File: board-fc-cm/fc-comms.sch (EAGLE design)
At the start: 251 parts, among them IC1 TPS79930QDDCRQ1, IC10 LNA_COMMON, IC11 MPU-9250, IC12 TXB0108PW, IC13 TPS3813K33-EP_DBV_6, IC14 TMP100-EP_DBV_6, IC15 LHA1+, IC16 PCT2075TP, IC17 MMZ09332BT1, IC18 PCT2075TP, IC2 TPS79930QDDCRQ1, IC3 MSP430FR2311PW, IC4 MCP1700TT, IC5 TXB0108PW, IC6 TXB0108PW, IC7 CC1125RHBT, IC77 74LVC1G08, IC8 CC1125RHBT, IC9 TM4C123[7,G]XXPM, J3 SWD_SHROUD, Q1 8MHz, Q2 BSS84, Q3 32.768kHz, Q4 BSS123, Q5 BSS84, X1 SHIELD-26X26, X10 BU-SMA-V, X11 BU-SMA-V, X12 BU-SMA-V, X13 BU-SMA-V, X14 BU-SMA-V, X15 BU-SMA-V, X16 BU-SMA-V, X17 BU-SMA-V, X18 BU-SMA-V, X2 SHIELD-26X26, X3 LFTCXO070, X4 LFTCXO070, X5 BU-SMA-V, X6 BU-SMA-V, X7 BU-SMA-V, X8 BU-SMA-V, X9 BU-SMA-V

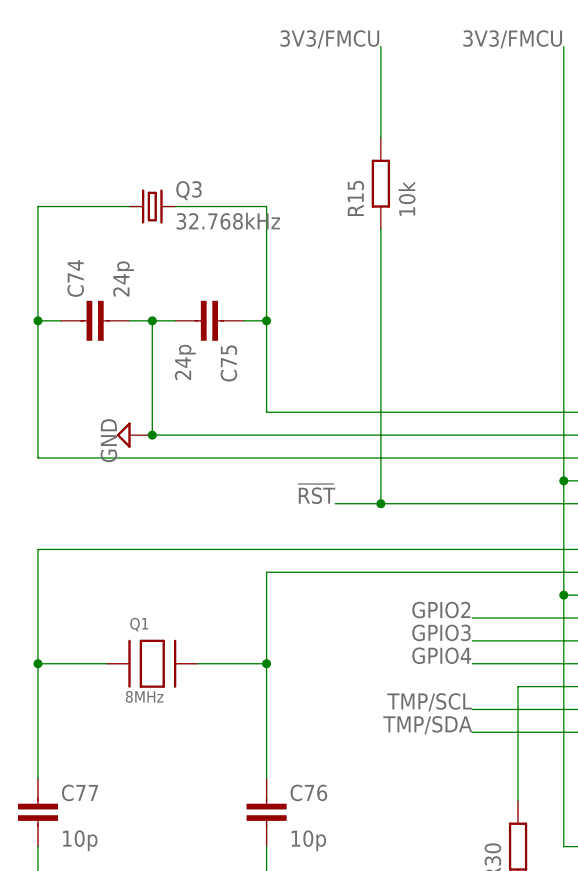
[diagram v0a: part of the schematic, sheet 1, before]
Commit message: adjusted crystal footprints
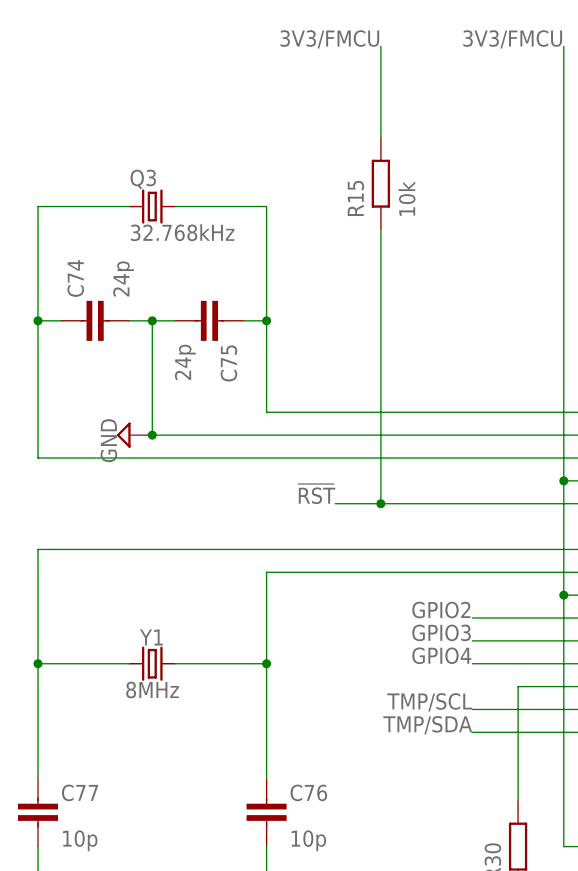
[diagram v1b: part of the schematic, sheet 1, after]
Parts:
- removed Q1: 8MHz, ti-tiva:ABM3
- added Y1: 8MHz, SparkFun-Clocks:CRYSTAL-8MHZSMD-5X3.2
- Q3: device crystal:CRYSTALTC26H -> cube-parts:RESONATOR_EPSON_FC_145; FARNELL (none) -> 2101347
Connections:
- removed net +5V: JP10.1, Q5.S, R22.P$2
- net 5V/SYS: now also JP10.1, Q5.S, R22.P$2
- net N$33: now also Y1.2; no longer Q1.P$1
- net N$8: now also Y1.1; no longer Q1.P$2
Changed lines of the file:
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@@
 <layer number="116" name="Patch_BOT" color="9" fill="4" visible="yes" active="yes"/>
 <layer number="118" name="Rect_Pads" color="7" fill="1" visible="no" active="yes"/>
+<layer number="120" name="120" color="7" fill="1" visible="yes" active="yes"/>
 <layer number="121" name="_tsilk" color="7" fill="1" visible="yes" active="yes"/>
 <layer number="122" name="_bsilk" color="7" fill="1" visible="yes" active="yes"/>
@@
 <layer number="132" name="bAdjust" color="7" fill="1" visible="yes" active="yes"/>
 <layer number="144" name="Drill_legend" color="7" fill="1" visible="yes" active="yes"/>
+<layer number="145" name="DrillLegend_01-16" color="2" fill="9" visible="yes" active="yes"/>
+<layer number="146" name="DrillLegend_01-20" color="3" fill="9" visible="yes" active="yes"/>
 <layer number="150" name="Notes" color="7" fill="1" visible="yes" active="yes"/>
 <layer number="151" name="HeatSink" color="7" fill="1" visible="yes" active="yes"/>
@@
 <part name="SUPPLY39" library="supply2" deviceset="GND" device=""/>
 <part name="SUPPLY41" library="supply2" deviceset="GND" device=""/>
-<part name="Q3" library="crystal" deviceset="CRYSTAL" device="TC26H" value="32.768kHz"/>
-<part name="Q1" library="ti-tiva" deviceset="ABM3" device="" value="8MHz"/>
+<part name="Q3" library="cube-parts" deviceset="RESONATOR_EPSON_FC_145" device="" value="32.768kHz">
+<attribute name="FARNELL" value="2101347"/>
+</part>
 <part name="SUPPLY1" library="supply2" deviceset="GND" device=""/>
 <part name="SUPPLY2" library="supply2" deviceset="GND" device=""/>
@@
 <part name="TP24" library="testpad" deviceset="PTR1" device="B1,27" value="PTR1B1,27"/>
 <part name="TP25" library="testpad" deviceset="PTR1" device="B1,27" value="PTR1B1,27"/>
+<part name="Y1" library="SparkFun-Clocks" deviceset="CRYSTAL-8MHZ" device="SMD-5X3.2" value="8MHz">
+<attribute name="FARNELL" value="2308726"/>
+</part>
 </parts>
 <sheets>
@@
 <instance part="SUPPLY39" gate="GND" x="106.68" y="127"/>
 <instance part="SUPPLY41" gate="GND" x="81.28" y="127"/>
-<instance part="Q3" gate="G$1" x="93.98" y="228.6"/>
-<instance part="Q1" gate="G$1" x="93.98" y="177.8"/>
+<instance part="Q3" gate="G$1" x="93.98" y="228.6">
+<attribute name="FARNELL" x="93.98" y="228.6" size="1.778" layer="96" display="off"/>
+</instance>
 <instance part="SUPPLY16" gate="GND" x="401.32" y="200.66"/>
 <instance part="SV2" gate="G$1" x="119.38" y="67.31" rot="MR180"/>
@@
 <instance part="SUPPLY30" gate="GND" x="134.62" y="137.16"/>
 <instance part="JP12" gate="G$1" x="408.94" y="223.52" rot="MR0"/>
+<instance part="Y1" gate="G$1" x="93.98" y="177.8">
+<attribute name="FARNELL" x="93.98" y="177.8" size="1.778" layer="96" display="off"/>
+</instance>
 </instances>
 <busses>
@@
 <net name="N$8" class="0">
 <segment>
-<wire x1="88.9" y1="177.8" x2="81.28" y2="177.8" width="0.1524" layer="91"/>
+<wire x1="91.44" y1="177.8" x2="81.28" y2="177.8" width="0.1524" layer="91"/>
 <pinref part="C77" gate="G$1" pin="1"/>
 <wire x1="81.28" y1="177.8" x2="81.28" y2="165.1" width="0.1524" layer="91"/>
@@
 <wire x1="81.28" y1="190.5" x2="81.28" y2="177.8" width="0.1524" layer="91"/>
 <junction x="81.28" y="177.8"/>
-<pinref part="Q1" gate="G$1" pin="P$2"/>
+<pinref part="Y1" gate="G$1" pin="1"/>
 </segment>
 </net>
@@
 <pinref part="C76" gate="G$1" pin="1"/>
 <wire x1="106.68" y1="177.8" x2="106.68" y2="165.1" width="0.1524" layer="91"/>
-<wire x1="106.68" y1="177.8" x2="99.06" y2="177.8" width="0.1524" layer="91"/>
+<wire x1="106.68" y1="177.8" x2="96.52" y2="177.8" width="0.1524" layer="91"/>
 <pinref part="IC9" gate="G$1" pin="OSC1"/>
 <wire x1="144.78" y1="187.96" x2="106.68" y2="187.96" width="0.1524" layer="91"/>
 <wire x1="106.68" y1="187.96" x2="106.68" y2="177.8" width="0.1524" layer="91"/>
 <junction x="106.68" y="177.8"/>
-<pinref part="Q1" gate="G$1" pin="P$1"/>
+<pinref part="Y1" gate="G$1" pin="2"/>
 </segment>
 </net>
@@
 </segment>
 </net>
-<net name="+5V" class="0">
-<segment>
-<pinref part="P+3" gate="1" pin="+5V"/>
-<pinref part="Q5" gate="G$1" pin="S"/>
-<wire x1="208.28" y1="114.3" x2="208.28" y2="116.84" width="0.1524" layer="91"/>
-<pinref part="R22" gate="G$1" pin="P$2"/>
-<wire x1="208.28" y1="116.84" x2="208.28" y2="124.46" width="0.1524" layer="91"/>
-<wire x1="208.28" y1="124.46" x2="208.28" y2="127" width="0.1524" layer="91"/>
-<wire x1="195.58" y1="121.92" x2="195.58" y2="124.46" width="0.1524" layer="91"/>
-<wire x1="195.58" y1="124.46" x2="208.28" y2="124.46" width="0.1524" layer="91"/>
-<junction x="208.28" y="124.46"/>
-<pinref part="JP10" gate="G$1" pin="1"/>
-<wire x1="220.98" y1="111.76" x2="220.98" y2="116.84" width="0.1524" layer="91"/>
-<wire x1="220.98" y1="116.84" x2="208.28" y2="116.84" width="0.1524" layer="91"/>
-<junction x="208.28" y="116.84"/>
-</segment>
-</net>
 <net name="N$57" class="0">
 <segment>
@@
 <label x="-66.04" y="-58.42" size="1.778" layer="95"/>
 </segment>
+<segment>
+<pinref part="P+3" gate="1" pin="+5V"/>
+<pinref part="Q5" gate="G$1" pin="S"/>
+<wire x1="208.28" y1="114.3" x2="208.28" y2="116.84" width="0.1524" layer="91"/>
+<pinref part="R22" gate="G$1" pin="P$2"/>
+<wire x1="208.28" y1="116.84" x2="208.28" y2="124.46" width="0.1524" layer="91"/>
+<wire x1="208.28" y1="124.46" x2="208.28" y2="127" width="0.1524" layer="91"/>
+<wire x1="195.58" y1="121.92" x2="195.58" y2="124.46" width="0.1524" layer="91"/>
+<wire x1="195.58" y1="124.46" x2="208.28" y2="124.46" width="0.1524" layer="91"/>
+<junction x="208.28" y="124.46"/>
+<pinref part="JP10" gate="G$1" pin="1"/>
+<wire x1="220.98" y1="111.76" x2="220.98" y2="116.84" width="0.1524" layer="91"/>
+<wire x1="220.98" y1="116.84" x2="208.28" y2="116.84" width="0.1524" layer="91"/>
+<junction x="208.28" y="116.84"/>
+</segment>
 </net>

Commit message: sent off
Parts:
- added JP13, JP14, JP4: JUMPER-SMT_2_NC_TRACE_SILK, SparkFun-Jumpers:JUMPER-SMT_2_NC_TRACE_SILK
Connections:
- removed net 3V3/BTC: SV2.52
- removed net 3V3/TC: SV2.51
- removed net GNSS/!RST: SV2.10
- new net 5V/RX: JP14.2, JP3.2, R1.P$1, SV2.51
- new net 5V/TX: JP10.1, JP13.2, JP2.1, Q5.S, R22.P$2, R3.P$1, SV2.52
- new net N$64: C11.1, IC4.OUT, JP4.1
- net 3V3/FMCU: now also JP4.2; no longer C11.1, IC4.OUT
- net 5V/SYS: now also JP13.1, JP14.1; no longer JP10.1, JP2.1, JP3.2, Q5.S, R1.P$1, R22.P$2, R3.P$1
- net GNSS/!RESETIN: now also SV2.10
